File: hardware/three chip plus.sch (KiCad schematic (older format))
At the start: 42 parts, among them J1 POWER, J2 PORT B, J3 PORT A, J4 Conn_01x10_Male, J5 ADDRESS BUS, J6 DATA BUS, J7 R/~W, SW1 RESET, U1 74LS14, U2 74LS32, U3 74LS08, U4 6522, U5 6502, U6 74LS138, U7 2716, U8 2114, U9 2114, X1 ACO-1MHz

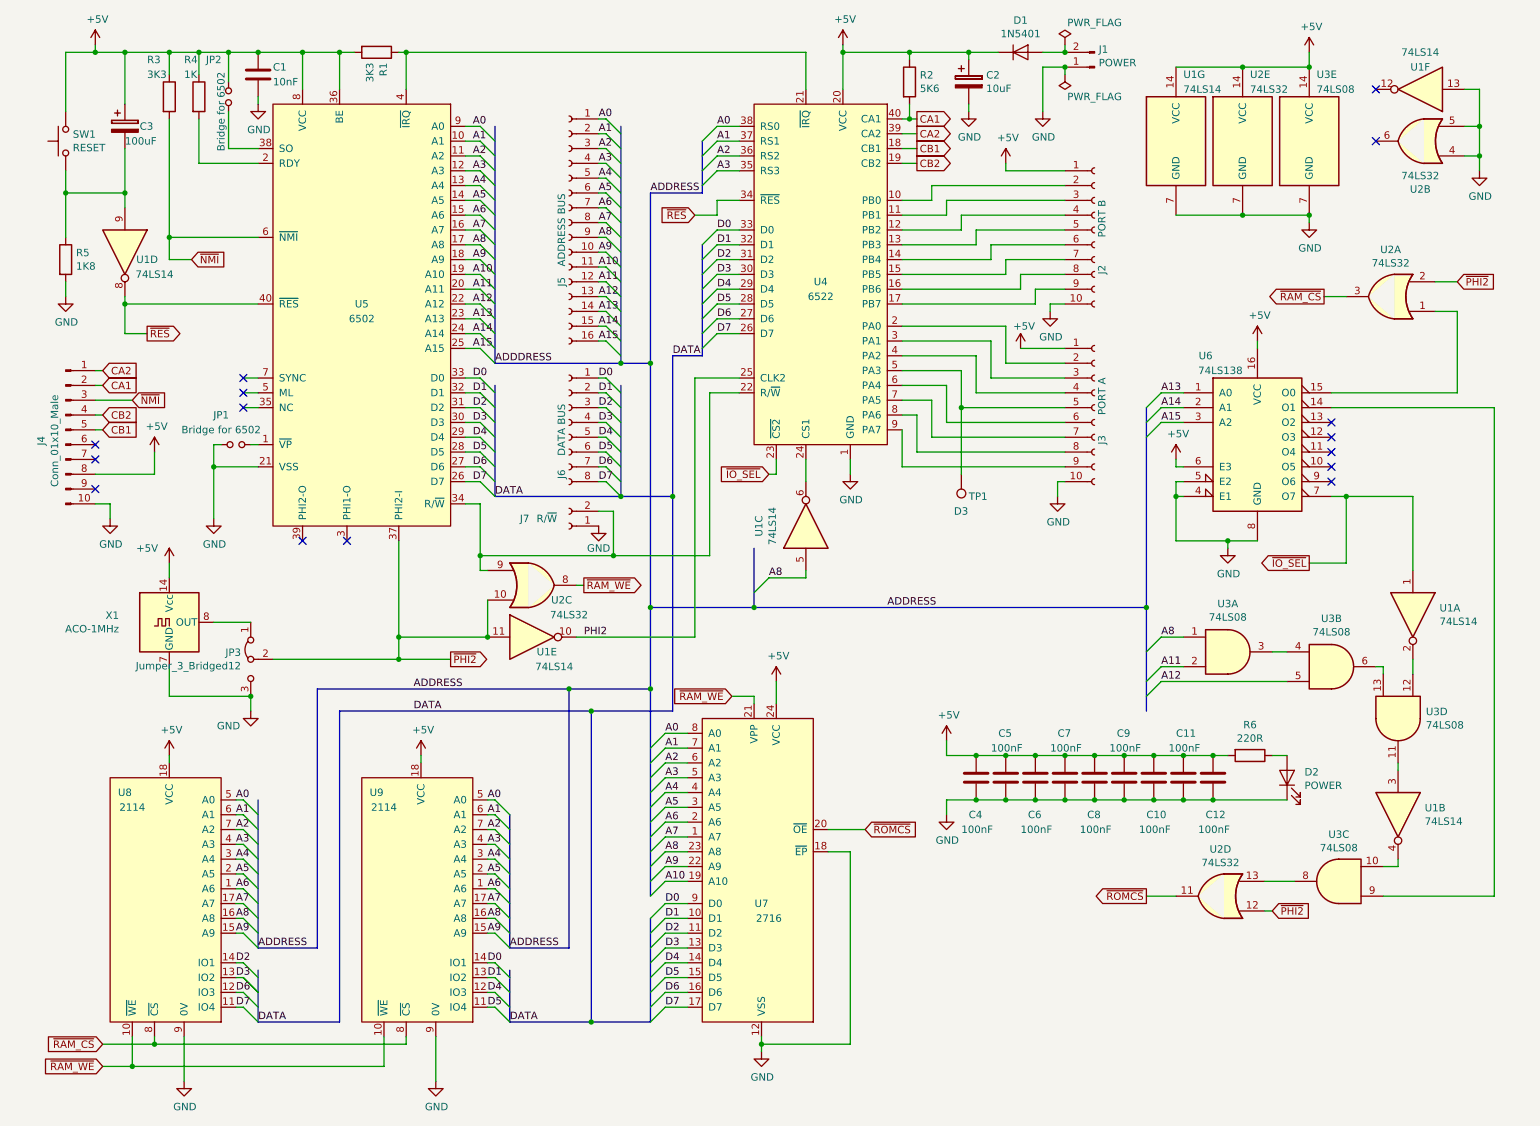
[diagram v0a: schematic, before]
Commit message: ISS2 Updates
Change log:
1. corrected error in PHI2/~PHI2~ clocks to U4 and U2 (schematic & PCB)
2. made D1 parallel protection to avoid volt drop on +5V rail
3. added missing R5, C2 legends (PCB)
4. corrected Power In legend polarity (PCB)
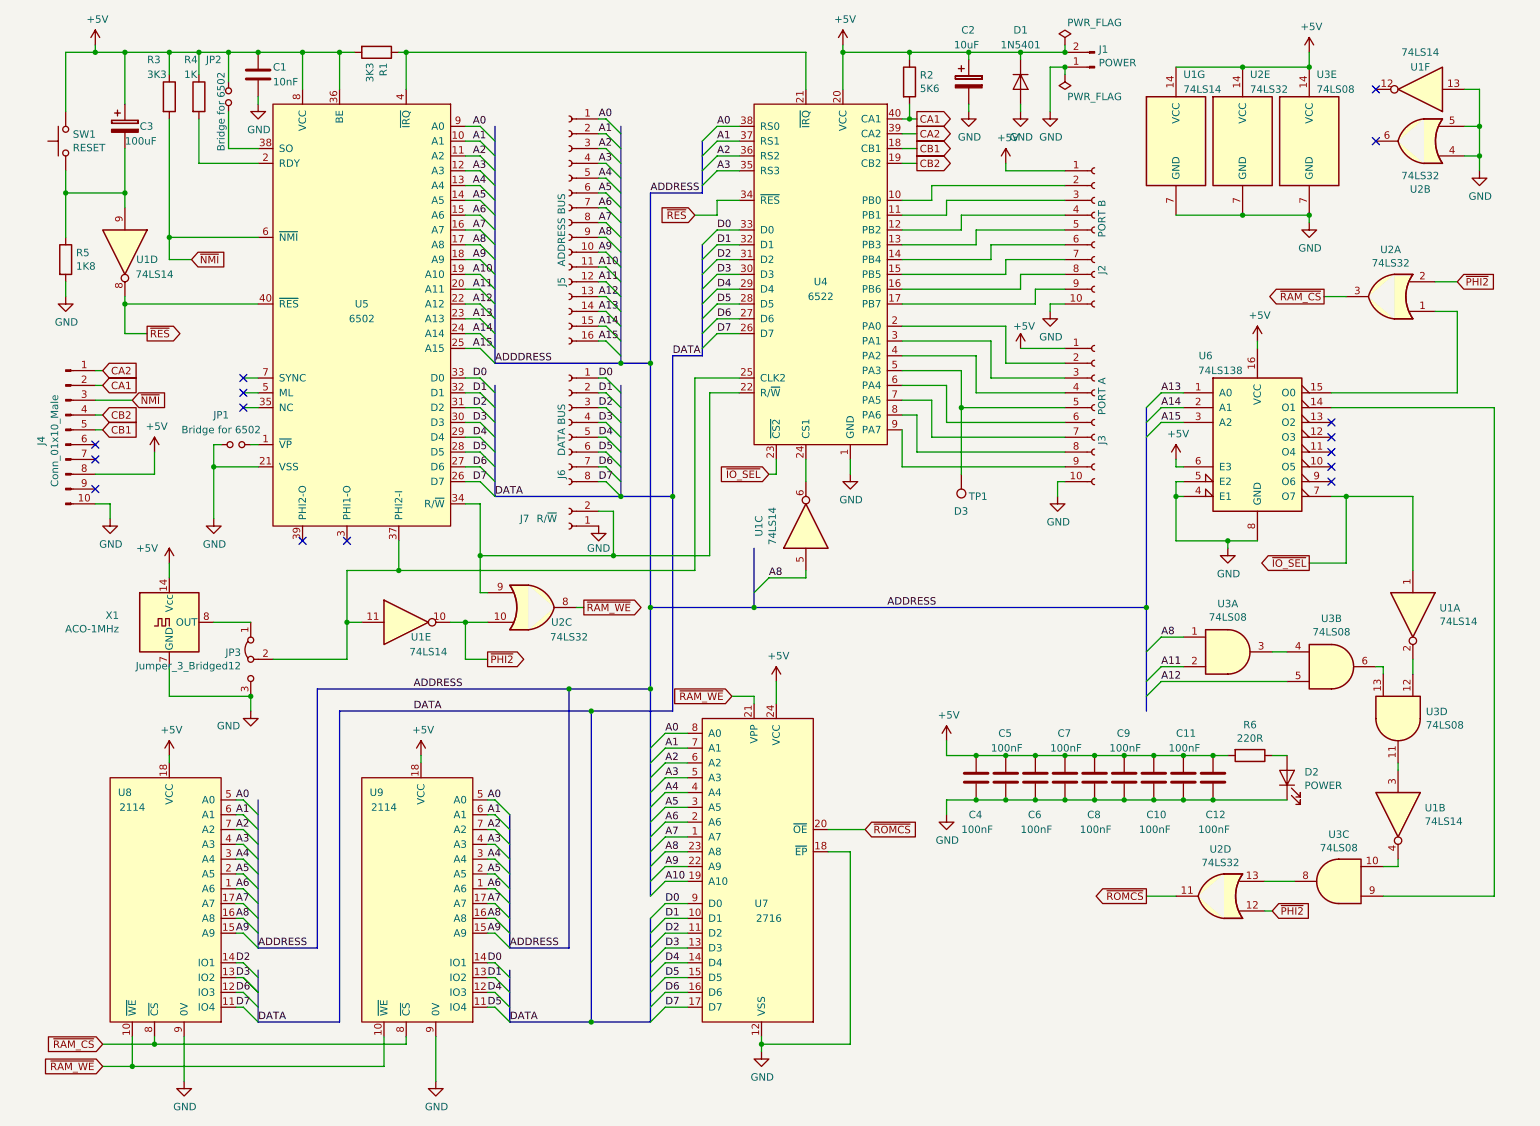
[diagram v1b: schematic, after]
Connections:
- net +5V: now also J1.2 (Pin_2)
- net GND: now also D1.2 (A)
- net ~PHI2: now also U1.10; no longer JP3.2 (C), U1.11, U5.37 (PHI2-I)
- net PHI2: no longer names the net of U4.25 (CLK2)
- net PHI2: now also JP3.2 (C), U1.11, U5.37 (PHI2-I); no longer U1.10
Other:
- moved on the sheet: D1, U1E, U2C
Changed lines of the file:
@@
 EESchema Schematic File Version 4
+LIBS:three chip plus-cache
 EELAYER 26 0
 EELAYER END
@@
 Sheet 1 1
 Title "UNILAB 3 CHIP PLUS CLONE"
-Date "2020-04-07"
-Rev "ISS1"
+Date "2021-05-31"
+Rev "ISS2"
 Comp ""
-Comment1 ""
-Comment2 ""
+Comment1 "2021-05-31 (ISS2): Corrected PHI2 clock to U4 and ~PHI2~ clock to U2A,C,D"
+Comment2 "2021-05-31 (ISS2): Made D1 parallel-reverse-protection to avoid forward volt drop"
 Comment3 "Note1: some corrections made over original schematic"
 Comment4 "clone by steve@croz.co.uk"
@@
 L 74xx:74LS14 U1
 U 5 1 5CCFCD38
-P 3850 4700
-F 0 "U1" H 3950 4600 50  0000 C CNN
-F 1 "74LS14" H 4000 4500 50  0000 C CNN
-F 2 "Package_DIP:DIP-14_W7.62mm_LongPads" H 3850 4700 50  0001 C CNN
-F 3 "http://www.ti.com/lit/gpn/sn74LS14" H 3850 4700 50  0001 C CNN
-	5    3850 4700
+P 3000 4600
+F 0 "U1" H 3100 4500 50  0000 C CNN
+F 1 "74LS14" H 3150 4400 50  0000 C CNN
+F 2 "Package_DIP:DIP-14_W7.62mm_LongPads" H 3000 4600 50  0001 C CNN
+F 3 "http://www.ti.com/lit/gpn/sn74LS14" H 3000 4600 50  0001 C CNN
+	5    3000 4600
 	1    0    0    -1
 $EndComp
@@
 L 74xx:74LS32 U2
 U 3 1 5CCFDFFF
-P 3850 4350
-F 0 "U2" H 4050 4250 50  0000 C CNN
-F 1 "74LS32" H 4100 4150 50  0000 C CNN
-F 2 "Package_DIP:DIP-14_W7.62mm_LongPads" H 3850 4350 50  0001 C CNN
-F 3 "http://www.ti.com/lit/gpn/sn74LS32" H 3850 4350 50  0001 C CNN
-	3    3850 4350
+P 3850 4500
+F 0 "U2" H 4050 4400 50  0000 C CNN
+F 1 "74LS32" H 4100 4300 50  0000 C CNN
+F 2 "Package_DIP:DIP-14_W7.62mm_LongPads" H 3850 4500 50  0001 C CNN
+F 3 "http://www.ti.com/lit/gpn/sn74LS32" H 3850 4500 50  0001 C CNN
+	3    3850 4500
 	1    0    0    -1
 $EndComp
@@
 L Device:D D1
 U 1 1 5CD01E03
-P 7150 750
-F 0 "D1" H 7150 966 50  0000 C CNN
-F 1 "1N5401" H 7150 875 50  0000 C CNN
-F 2 "Diode_THT:D_DO-201AD_P12.70mm_Horizontal" H 7150 750 50  0001 C CNN
-F 3 "~" H 7150 750 50  0001 C CNN
-	1    7150 750
-	1    0    0    -1
+P 7150 950
+F 0 "D1" V 6800 950 50  0000 C CNN
+F 1 "1N5401" V 6900 950 50  0000 C CNN
+F 2 "Diode_THT:D_DO-201AD_P12.70mm_Horizontal" H 7150 950 50  0001 C CNN
+F 3 "~" H 7150 950 50  0001 C CNN
+	1    7150 950
+	0    1    1    0
 $EndComp
 $Comp
@@
 U 1 1 5CD028EB
 P 6800 950
-F 0 "C2" H 6918 996 50  0000 L CNN
-F 1 "10uF" H 6918 905 50  0000 L CNN
+F 0 "C2" H 6750 1300 50  0000 L CNN
+F 1 "10uF" H 6700 1200 50  0000 L CNN
 F 2 "Capacitor_THT:CP_Radial_D4.0mm_P1.50mm" H 6838 800 50  0001 C CNN
 F 3 "~" H 6800 950 50  0001 C CNN
@@
 	5250 2950 4950 2950
 Wire Wire Line
-	4950 2950 4950 4700
+	4950 2950 4950 4250
 Text Label 6250 4500 0    50   ~ 0
 ADDRESS
-Wire Wire Line
-	7000 750  6800 750
 $Comp
 L Connector:Conn_01x02_Male J1
@@
 L power:GND #PWR0117
 U 1 1 5EEE0114
-P 7300 1150
-F 0 "#PWR0117" H 7300 900 50  0001 C CNN
-F 1 "GND" H 7305 977 50  0000 C CNN
-F 2 "" H 7300 1150 50  0001 C CNN
-F 3 "" H 7300 1150 50  0001 C CNN
-	1    7300 1150
-	1    0    0    -1
-$EndComp
-Wire Wire Line
-	7450 750  7300 750
-Wire Wire Line
-	7450 850  7300 850
-Wire Wire Line
-	7300 850  7300 1150
+P 7350 1150
+F 0 "#PWR0117" H 7350 900 50  0001 C CNN
+F 1 "GND" H 7355 977 50  0000 C CNN
+F 2 "" H 7350 1150 50  0001 C CNN
+F 3 "" H 7350 1150 50  0001 C CNN
+	1    7350 1150
+	1    0    0    -1
+$EndComp
+Wire Wire Line
+	7450 850  7350 850
+Wire Wire Line
+	7350 850  7350 1150
 $Comp
 L power:+5V #PWR0118
@@
 Text Label 3700 7300 0    50   ~ 0
 DATA
-Text GLabel 4200 4350 2    50   Output ~ 0
+Text GLabel 4200 4500 2    50   Output ~ 0
 ~RAM_WE
 Text GLabel 950  7600 0    50   Input ~ 0
@@
 Wire Wire Line
 	5350 5100 5350 5150
-Text GLabel 3300 4850 2    50   Output ~ 0
+Text GLabel 3550 4850 2    50   Output ~ 0
 ~PHI2
 Text GLabel 10100 2300 2    50   Input ~ 0
@@
 Wire Wire Line
 	10250 1450 10250 1250
-Wire Wire Line
-	3550 4450 3550 4700
-Wire Wire Line
-	2950 4850 3300 4850
 $Comp
 L power:+5V #PWR0126
@@
 Wire Wire Line
 	5450 3600 5500 3600
-Text Label 4200 4700 0    50   ~ 0
-PHI2
 NoConn ~ 9550 1350
 $Comp
@@
 	1950 3400 2000 3400
 Wire Wire Line
-	4150 4700 4950 4700
-Wire Wire Line
 	3000 750  5700 750
 Connection ~ 3000 750
@@
 Wire Wire Line
 	3500 3800 3500 4150
-Connection ~ 3500 4150
 Connection ~ 4250 7300
 Wire Bus Line
@@
 Text Label 3050 5200 0    50   ~ 0
 DATA
-Connection ~ 6800 750
 Wire Wire Line
 	5950 750  6400 750
@@
 NoConn ~ 2600 4050
 Wire Wire Line
-	4200 4350 4150 4350
+	4200 4500 4150 4500
 Wire Wire Line
 	2000 3550 1700 3550
@@
 Wire Wire Line
 	1400 4200 1400 4300
-Wire Wire Line
-	2950 4050 2950 4700
-Connection ~ 2950 4850
-Wire Wire Line
-	3550 4700 2950 4700
-Connection ~ 3550 4700
-Connection ~ 2950 4700
-Wire Wire Line
-	2950 4700 2950 4850
-Wire Wire Line
-	2100 4850 2950 4850
 $Comp
 L Device:C C4
@@
 $EndComp
 Wire Wire Line
-	3500 4150 3500 4250
-Wire Wire Line
-	3550 4250 3500 4250
+	3550 4400 3500 4400
 Text Label 4300 3650 0    50   ~ 0
 D7
@@
 Wire Wire Line
 	7450 700  7450 750
-Connection ~ 7450 750
 $Comp
 L Device:LED D2
@@
 Wire Wire Line
 	6750 3600 6750 3150
+Wire Wire Line
+	7150 800  7150 750
+Wire Wire Line
+	7150 750  7450 750
+Connection ~ 7450 750
+Wire Wire Line
+	7150 750  6800 750
+Connection ~ 7150 750
+Connection ~ 6800 750
+$Comp
+L power:GND #PWR0128
+U 1 1 60CCABBE
+P 7150 1150
+F 0 "#PWR0128" H 7150 900 50  0001 C CNN
+F 1 "GND" H 7155 977 50  0000 C CNN
+F 2 "" H 7150 1150 50  0001 C CNN
+F 3 "" H 7150 1150 50  0001 C CNN
+	1    7150 1150
+	1    0    0    -1
+$EndComp
+Wire Wire Line
+	7150 1100 7150 1150
+Wire Wire Line
+	3300 4600 3400 4600
+Wire Wire Line
+	3550 4850 3400 4850
+Wire Wire Line
+	3400 4850 3400 4600
+Connection ~ 3400 4600
+Wire Wire Line
+	3400 4600 3550 4600
+Wire Wire Line
+	3500 4150 3500 4400
+Connection ~ 3500 4150
+Wire Wire Line
+	4950 4250 2950 4250
+Wire Wire Line
+	2950 4250 2950 4050
+Wire Wire Line
+	2100 4850 2600 4850
+Wire Wire Line
+	2600 4850 2600 4600
+Wire Wire Line
+	2600 4600 2700 4600
+Wire Wire Line
+	2600 4600 2600 4250
+Wire Wire Line
+	2600 4250 2950 4250
+Connection ~ 2600 4600
+Connection ~ 2950 4250
 Wire Bus Line
 	5350 4100 5350 4500
